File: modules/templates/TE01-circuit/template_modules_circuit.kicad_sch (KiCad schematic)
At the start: 6 parts, among them J1 MODULE Connector

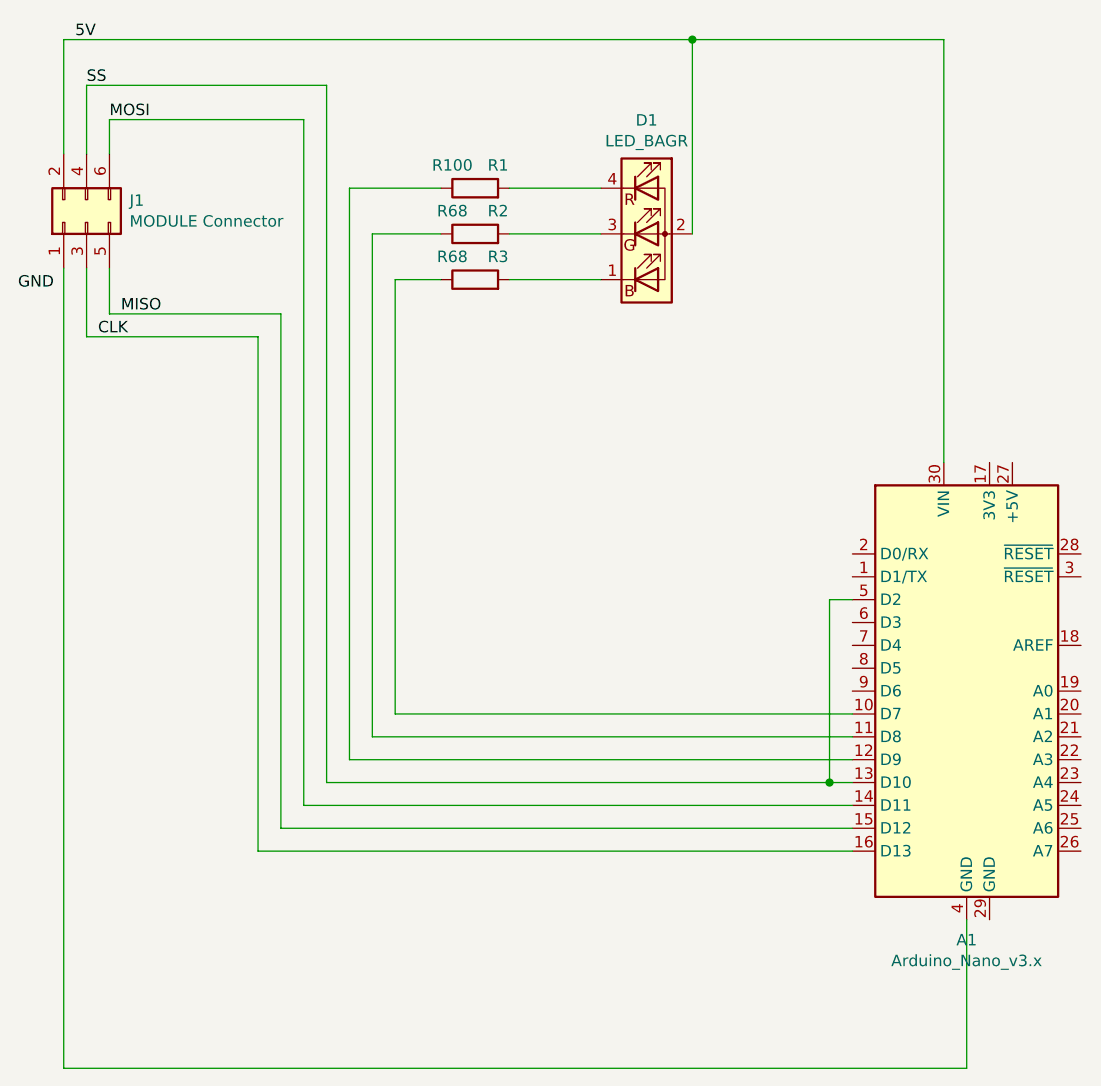
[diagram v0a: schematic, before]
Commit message: cleanup circuit
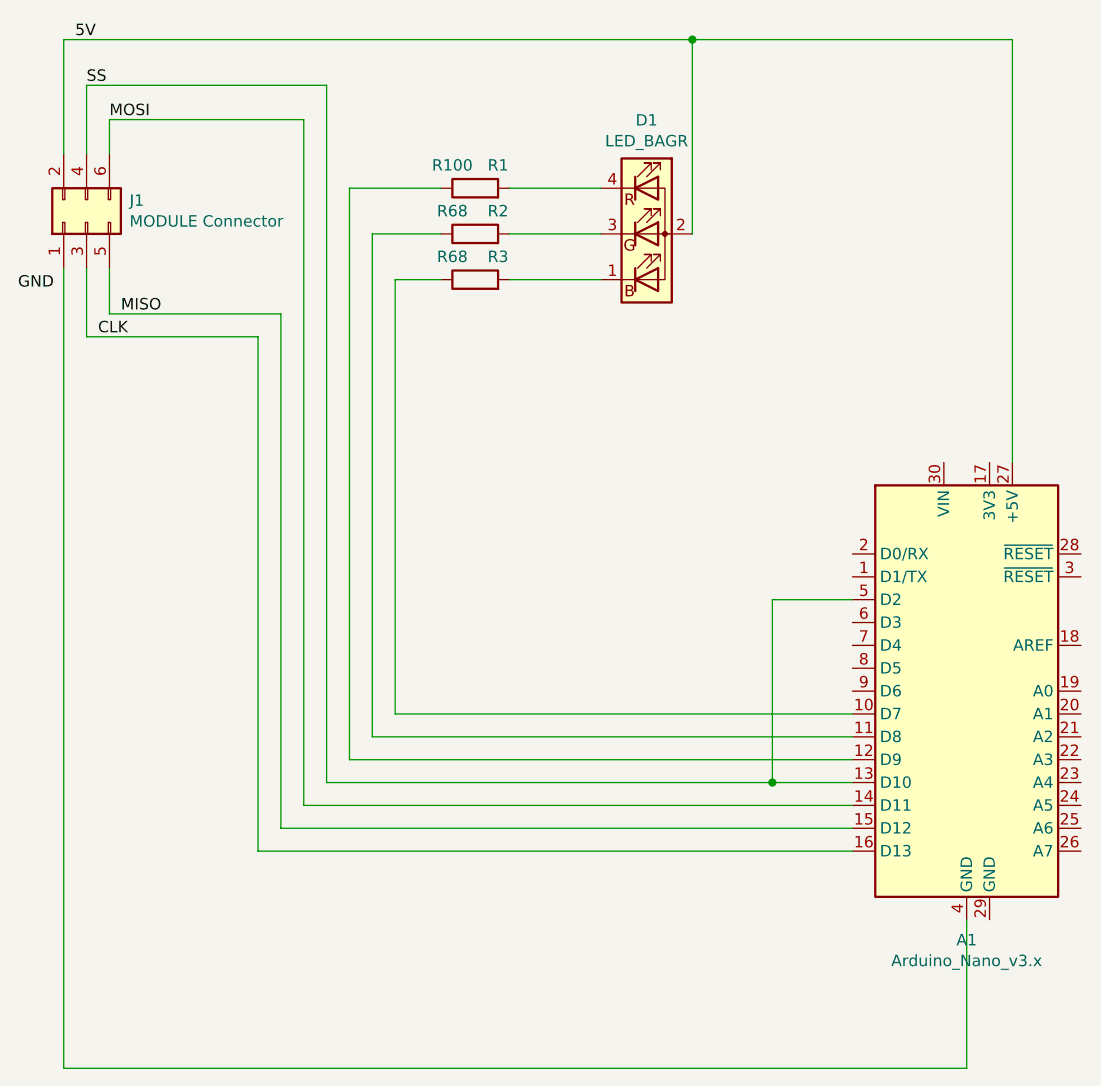
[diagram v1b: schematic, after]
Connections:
- net 5V: now also A1.27 (+5V); no longer A1.30 (VIN)
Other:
- title: (none) -> Schaltplan Modul Template (XX)
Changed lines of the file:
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@@
 (kicad_sch (version 20211123) (generator eeschema)
   (paper "A4")
-  (junction (at 127 120.65) (diameter 0) (color 0 0 0 0)
+  (title_block
+    (title "Schaltplan Modul Template (XX)")
+    (date "14.12.2022")
+  )
+  (junction (at 120.65 120.65) (diameter 0) (color 0 0 0 0)
   )
   (junction (at 111.76 38.1) (diameter 0) (color 0 0 0 0)
@@
     (stroke (width 0) (type default) (color 0 0 0 0))
   )
-  (wire (pts (xy 139.7 38.1) (xy 139.7 85.09))
+  (wire (pts (xy 111.76 38.1) (xy 147.32 38.1))
     (stroke (width 0) (type default) (color 0 0 0 0))
   )
@@
     (stroke (width 0) (type default) (color 0 0 0 0))
   )
-  (wire (pts (xy 71.12 120.65) (xy 127 120.65))
-    (stroke (width 0) (type default) (color 0 0 0 0))
-  )
-  (wire (pts (xy 127 120.65) (xy 129.54 120.65))
+  (wire (pts (xy 71.12 120.65) (xy 120.65 120.65))
     (stroke (width 0) (type default) (color 0 0 0 0))
   )
@@
     (stroke (width 0) (type default) (color 0 0 0 0))
   )
-  (wire (pts (xy 127 100.33) (xy 129.54 100.33))
-    (stroke (width 0) (type default) (color 0 0 0 0))
-  )
   (wire (pts (xy 68.58 46.99) (xy 68.58 123.19))
     (stroke (width 0) (type default) (color 0 0 0 0))
@@
     (stroke (width 0) (type default) (color 0 0 0 0))
   )
+  (wire (pts (xy 120.65 120.65) (xy 129.54 120.65))
+    (stroke (width 0) (type default) (color 0 0 0 0))
+  )
   (wire (pts (xy 129.54 118.11) (xy 73.66 118.11))
     (stroke (width 0) (type default) (color 0 0 0 0))
@@
     (stroke (width 0) (type default) (color 0 0 0 0))
   )
-  (wire (pts (xy 111.76 38.1) (xy 139.7 38.1))
+  (wire (pts (xy 120.65 100.33) (xy 129.54 100.33))
+    (stroke (width 0) (type default) (color 0 0 0 0))
+  )
+  (wire (pts (xy 120.65 120.65) (xy 120.65 100.33))
+    (stroke (width 0) (type default) (color 0 0 0 0))
+  )
+  (wire (pts (xy 147.32 38.1) (xy 147.32 85.09))
     (stroke (width 0) (type default) (color 0 0 0 0))
   )
@@
     (stroke (width 0) (type default) (color 0 0 0 0))
   )
-  (wire (pts (xy 127 120.65) (xy 127 100.33))
-    (stroke (width 0) (type default) (color 0 0 0 0))
-  )
